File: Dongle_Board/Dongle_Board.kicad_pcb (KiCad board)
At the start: 2 copper layers, 45 x 18.5 mm, 21 parts, among them P1 USB_A, U1 TCR2EF33, U2 ATMEGA32U4RC-A, U3 nRF24L01+, Y1 ABLS-8.000MHZ-B4-T

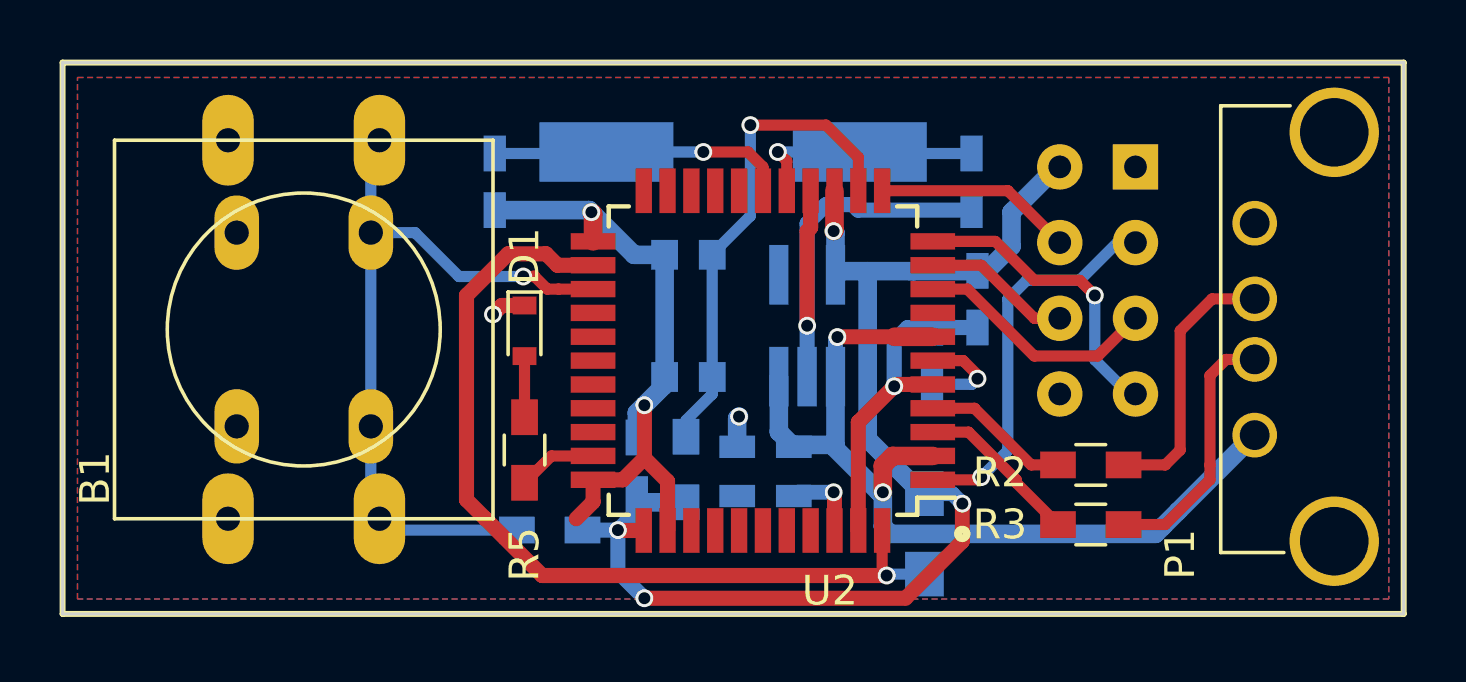
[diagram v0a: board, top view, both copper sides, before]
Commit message: Updated Dongle and Controller boards, ready for fab
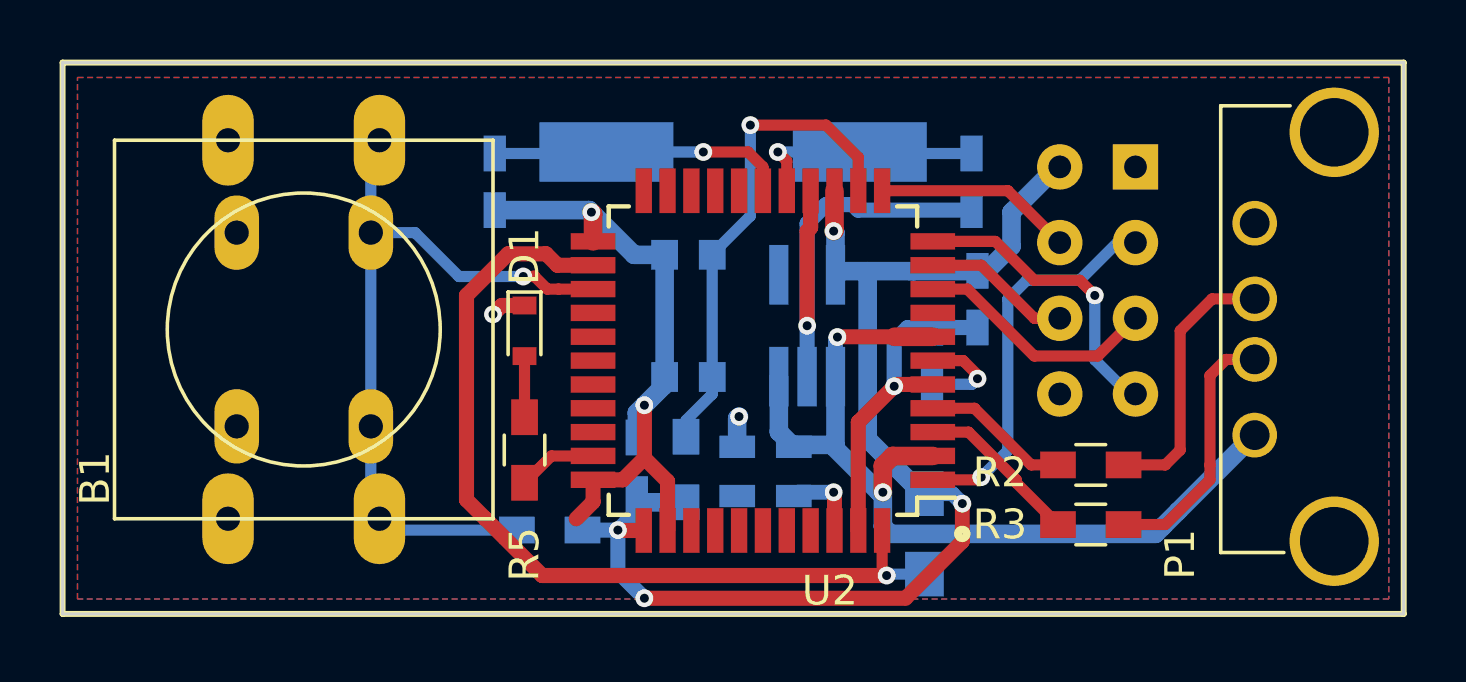
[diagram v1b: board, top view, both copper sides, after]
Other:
- net class Default: via_drill 0.4 -> 0.3
